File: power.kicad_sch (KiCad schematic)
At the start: 20 parts, among them J1 Conn_01x02, J2 USB-TYPE-C-008, U2 TLV70033_SOT23-5, U6 BQ24079RGT

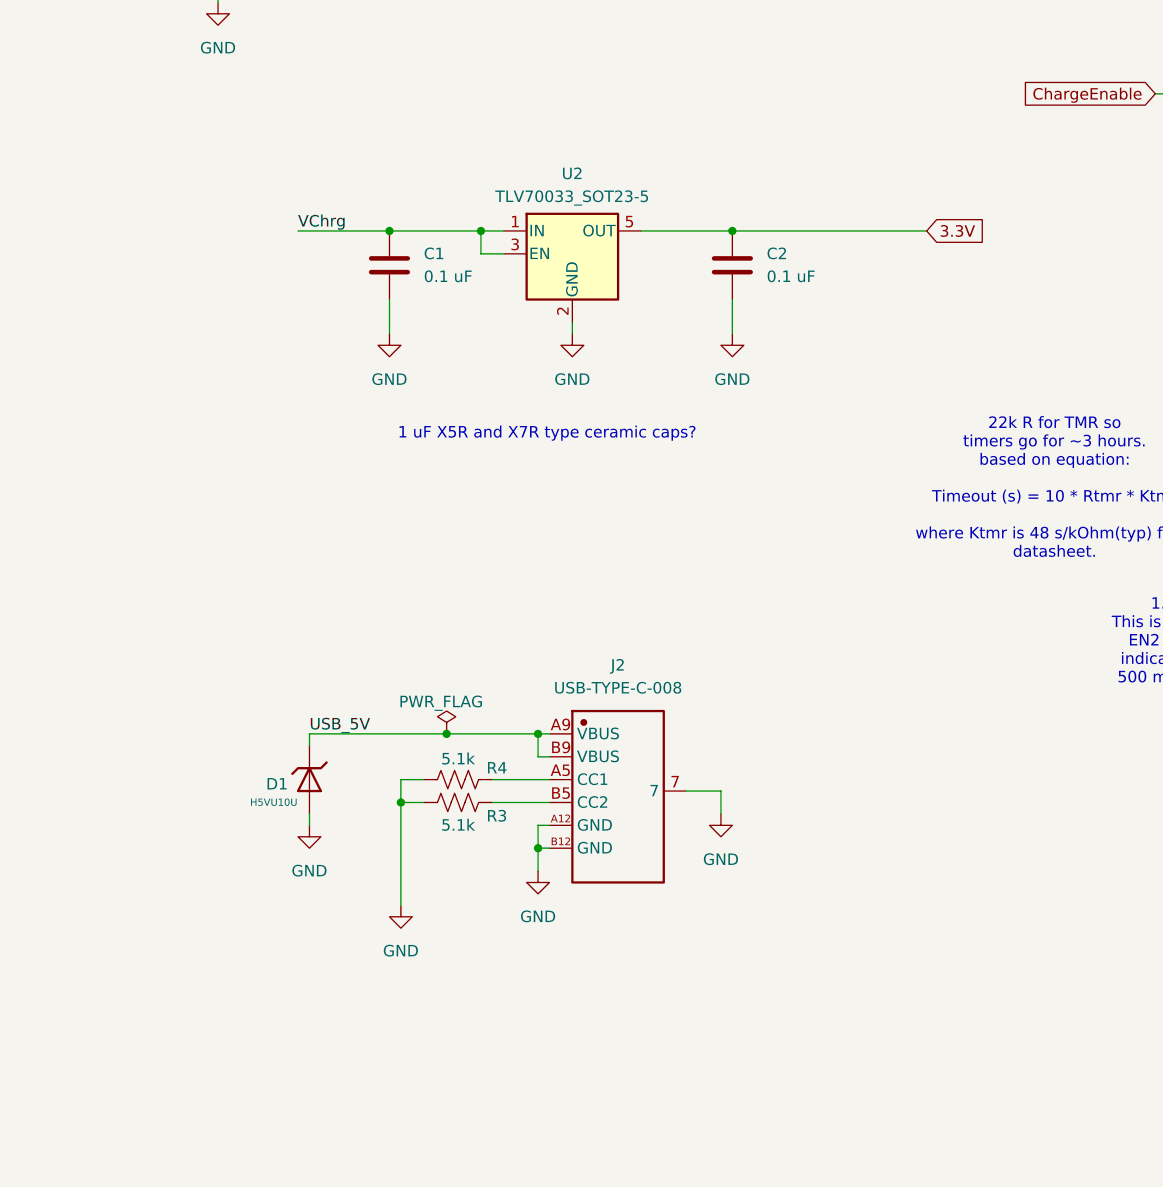
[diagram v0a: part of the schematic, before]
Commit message: update to include footprints from project specific lib
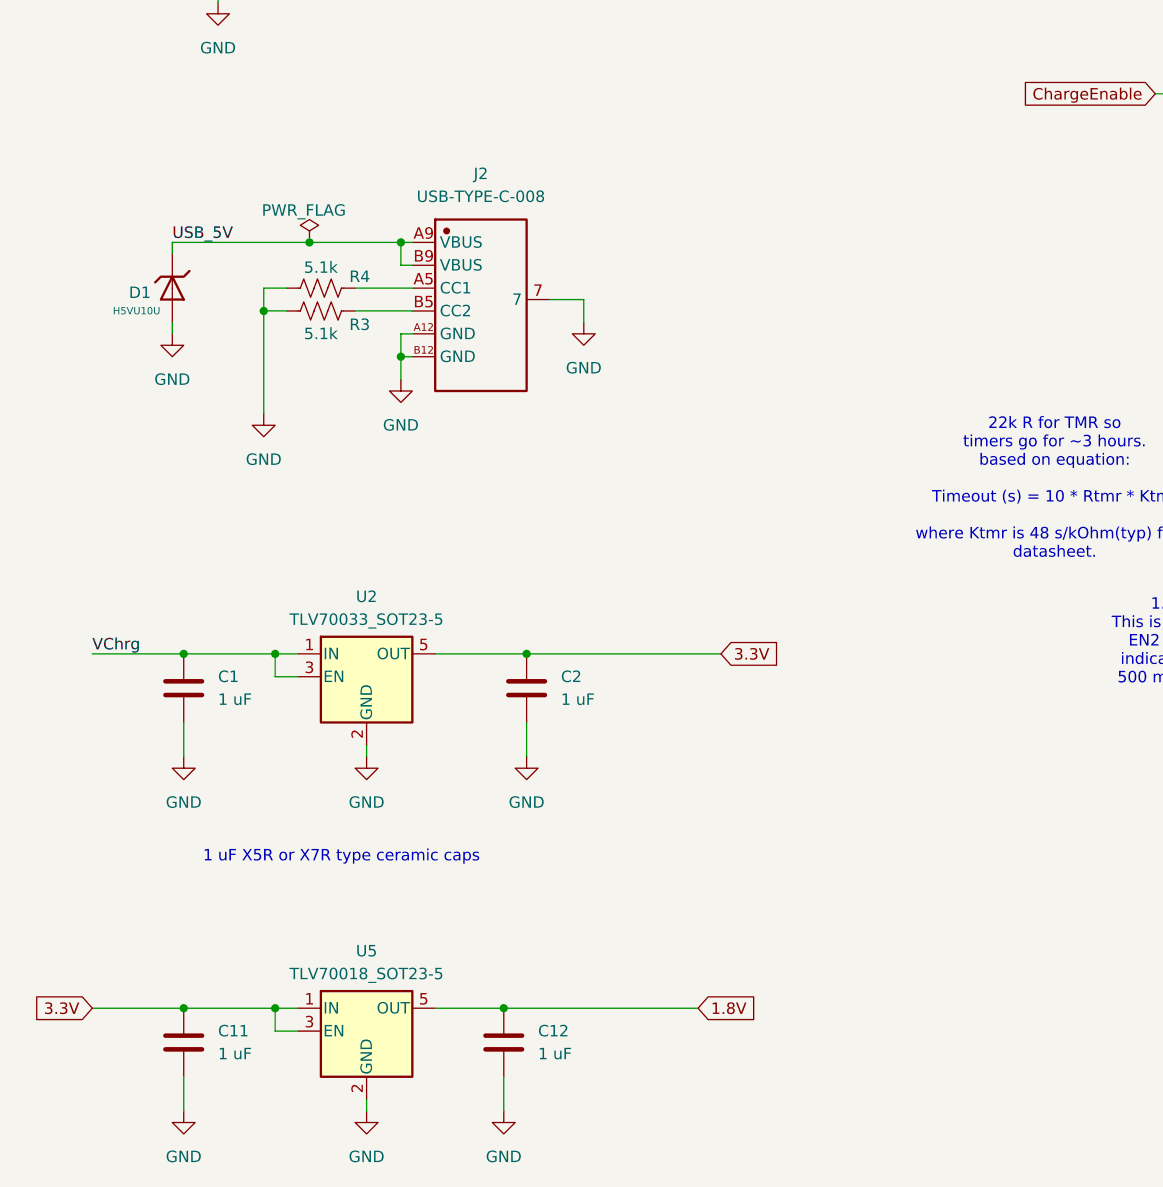
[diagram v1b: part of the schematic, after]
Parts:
- added C11, C12: 1 uF, PCM_JLCPCB:C_0402, symbol Device:C
- added U5: TLV70018_SOT23-5, Package_TO_SOT_SMD:SOT-23-5, symbol Regulator_Linear:TLV70018_SOT23-5
- C1, C2: value 0.1 uF -> 1 uF
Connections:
- net 3.3V: now also C11.1, U5.1 (IN), U5.3 (EN)
- net GND: now also C11.2, C12.2, U5.2 (GND)
- new net 1.8V: C12.1, U5.5 (OUT)
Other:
- note added: "1 uF X5R or X7R type ceramic caps"
- note removed: "1 uF X5R and X7R type ceramic caps?"
- moved on the sheet: C1, C2, D1, J2, R3, R4, U2
